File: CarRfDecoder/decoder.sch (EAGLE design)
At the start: 50 parts, among them T1 BC847, T2 BC847, T3 IRLML6402, U1 ATMEGA32U4TQFP-44, U2 RFM69CW, U3 MCP73831, U6 MIC5219 3.3V

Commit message: changes in the design
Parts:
- added C5, C6: 22pF, SparkFun-Capacitors:CAP0805
- added R12: 2K, SparkFun-Resistors:RESISTOR0603-RES
- added RST, XTAL, XTAL1: (no value), wirepad:SMD2
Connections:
- new net N$3: C5.2, U1.XTAL1, XTAL.P
- new net N$4: C6.2, U1.XTAL2, XTAL1.P
- new net N$5: R12.1, RST.P, U1.!RESET
- net GND: now also C5.1, C6.1
- net VCC: now also R12.2; no longer U1.!RESET
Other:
- moved on the sheet: C1
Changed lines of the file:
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@@
 <part name="SUPPLY1" library="SparkFun-Aesthetics" deviceset="VCC" device="" value="3.3V"/>
 <part name="AUX10" library="wirepad" deviceset="SMD2" device=""/>
+<part name="XTAL" library="wirepad" deviceset="SMD2" device=""/>
+<part name="XTAL1" library="wirepad" deviceset="SMD2" device=""/>
+<part name="C5" library="SparkFun-Capacitors" deviceset="CAP" device="0805" value="22pF"/>
+<part name="C6" library="SparkFun-Capacitors" deviceset="CAP" device="0805" value="22pF"/>
+<part name="GND3" library="SparkFun-Aesthetics" deviceset="GND" device=""/>
+<part name="R12" library="SparkFun-Resistors" deviceset="RESISTOR" device="0603-RES" value="2K"/>
+<part name="RST" library="wirepad" deviceset="SMD2" device=""/>
 </parts>
 <sheets>
@@
 <instance part="GND1" gate="1" x="20.32" y="10.16"/>
 <instance part="GND2" gate="1" x="20.32" y="27.94"/>
-<instance part="C1" gate="G$1" x="7.62" y="38.1"/>
+<instance part="C1" gate="G$1" x="-10.16" y="38.1"/>
 <instance part="USBV+" gate="1" x="-35.56" y="116.84"/>
 <instance part="USBD+" gate="1" x="-35.56" y="111.76"/>
@@
 <instance part="SUPPLY1" gate="G$1" x="27.94" y="-10.16"/>
 <instance part="AUX10" gate="1" x="220.98" y="-78.74" rot="MR0"/>
+<instance part="XTAL" gate="1" x="17.78" y="40.64"/>
+<instance part="XTAL1" gate="1" x="17.78" y="35.56"/>
+<instance part="C5" gate="G$1" x="10.16" y="43.18" rot="R90"/>
+<instance part="C6" gate="G$1" x="10.16" y="33.02" rot="R90"/>
+<instance part="GND3" gate="1" x="2.54" y="40.64"/>
+<instance part="R12" gate="G$1" x="30.48" y="96.52" rot="R90"/>
+<instance part="RST" gate="1" x="43.18" y="96.52" rot="R180"/>
 </instances>
 <busses>
@@
 <pinref part="U1" gate="G$1" pin="VCC@14"/>
 <wire x1="25.4" y1="83.82" x2="30.48" y2="83.82" width="0.1524" layer="91"/>
-<wire x1="25.4" y1="83.82" x2="25.4" y2="86.36" width="0.1524" layer="91"/>
 <junction x="25.4" y="83.82"/>
-<pinref part="U1" gate="G$1" pin="!RESET"/>
-<wire x1="25.4" y1="86.36" x2="30.48" y2="86.36" width="0.1524" layer="91"/>
 <wire x1="20.32" y1="83.82" x2="25.4" y2="83.82" width="0.1524" layer="91"/>
 <pinref part="U1" gate="G$1" pin="AVCC@24"/>
@@
 <junction x="25.4" y="81.28"/>
 <label x="15.24" y="86.36" size="1.778" layer="95"/>
+<pinref part="R12" gate="G$1" pin="2"/>
+<wire x1="30.48" y1="101.6" x2="25.4" y2="101.6" width="0.1524" layer="91"/>
+<wire x1="25.4" y1="101.6" x2="25.4" y2="83.82" width="0.1524" layer="91"/>
 </segment>
 <segment>
@@
 <pinref part="C1" gate="G$1" pin="2"/>
 <wire x1="30.48" y1="22.86" x2="20.32" y2="22.86" width="0.1524" layer="91"/>
-<wire x1="20.32" y1="22.86" x2="7.62" y2="22.86" width="0.1524" layer="91"/>
-<wire x1="7.62" y1="22.86" x2="7.62" y2="35.56" width="0.1524" layer="91"/>
+<wire x1="20.32" y1="22.86" x2="-10.16" y2="22.86" width="0.1524" layer="91"/>
+<wire x1="-10.16" y1="22.86" x2="-10.16" y2="35.56" width="0.1524" layer="91"/>
 <junction x="20.32" y="22.86"/>
 <wire x1="20.32" y1="22.86" x2="20.32" y2="15.24" width="0.1524" layer="91"/>
@@
 <pinref part="GND12" gate="1" pin="GND"/>
 </segment>
+<segment>
+<pinref part="C5" gate="G$1" pin="1"/>
+<pinref part="GND3" gate="1" pin="GND"/>
+<wire x1="5.08" y1="43.18" x2="2.54" y2="43.18" width="0.1524" layer="91"/>
+<pinref part="C6" gate="G$1" pin="1"/>
+<wire x1="5.08" y1="33.02" x2="5.08" y2="43.18" width="0.1524" layer="91"/>
+<junction x="5.08" y="43.18"/>
+</segment>
 </net>
 <net name="N$1" class="0">
@@
 <pinref part="U1" gate="G$1" pin="UCAP"/>
 <pinref part="C1" gate="G$1" pin="1"/>
-<wire x1="30.48" y1="58.42" x2="7.62" y2="58.42" width="0.1524" layer="91"/>
-<wire x1="7.62" y1="58.42" x2="7.62" y2="43.18" width="0.1524" layer="91"/>
+<wire x1="30.48" y1="58.42" x2="-10.16" y2="58.42" width="0.1524" layer="91"/>
+<wire x1="-10.16" y1="58.42" x2="-10.16" y2="43.18" width="0.1524" layer="91"/>
 </segment>
 </net>
@@
 </segment>
 </net>
+<net name="N$3" class="0">
+<segment>
+<pinref part="XTAL" gate="1" pin="P"/>
+<pinref part="U1" gate="G$1" pin="XTAL1"/>
+<wire x1="20.32" y1="40.64" x2="22.86" y2="40.64" width="0.1524" layer="91"/>
+<pinref part="C5" gate="G$1" pin="2"/>
+<wire x1="22.86" y1="40.64" x2="30.48" y2="40.64" width="0.1524" layer="91"/>
+<wire x1="12.7" y1="43.18" x2="22.86" y2="43.18" width="0.1524" layer="91"/>
+<wire x1="22.86" y1="43.18" x2="22.86" y2="40.64" width="0.1524" layer="91"/>
+<junction x="22.86" y="40.64"/>
+</segment>
+</net>
+<net name="N$4" class="0">
+<segment>
+<pinref part="XTAL1" gate="1" pin="P"/>
+<pinref part="U1" gate="G$1" pin="XTAL2"/>
+<wire x1="20.32" y1="35.56" x2="22.86" y2="35.56" width="0.1524" layer="91"/>
+<pinref part="C6" gate="G$1" pin="2"/>
+<wire x1="22.86" y1="35.56" x2="30.48" y2="35.56" width="0.1524" layer="91"/>
+<wire x1="12.7" y1="33.02" x2="22.86" y2="33.02" width="0.1524" layer="91"/>
+<wire x1="22.86" y1="33.02" x2="22.86" y2="35.56" width="0.1524" layer="91"/>
+<junction x="22.86" y="35.56"/>
+</segment>
+</net>
+<net name="N$5" class="0">
+<segment>
+<pinref part="R12" gate="G$1" pin="1"/>
+<pinref part="U1" gate="G$1" pin="!RESET"/>
+<wire x1="30.48" y1="91.44" x2="30.48" y2="86.36" width="0.1524" layer="91"/>
+<pinref part="RST" gate="1" pin="P"/>
+<wire x1="40.64" y1="96.52" x2="35.56" y2="96.52" width="0.1524" layer="91"/>
+<wire x1="35.56" y1="96.52" x2="35.56" y2="91.44" width="0.1524" layer="91"/>
+<wire x1="35.56" y1="91.44" x2="30.48" y2="91.44" width="0.1524" layer="91"/>
+<junction x="30.48" y="91.44"/>
+</segment>
+</net>

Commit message: Ready boards.
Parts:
- added VJ, VJ1: (no value), wirepad:SMD2
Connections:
- new net N$31: U2.3.3V, VJ.P
- net VCC: now also VJ1.P; no longer U2.3.3V
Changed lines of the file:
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@@
 <part name="R12" library="SparkFun-Resistors" deviceset="RESISTOR" device="0603-RES" value="2K"/>
 <part name="RST" library="wirepad" deviceset="SMD2" device=""/>
+<part name="VJ" library="wirepad" deviceset="SMD2" device=""/>
+<part name="VJ1" library="wirepad" deviceset="SMD2" device=""/>
 </parts>
 <sheets>
@@
 <instance part="R12" gate="G$1" x="30.48" y="96.52" rot="R90"/>
 <instance part="RST" gate="1" x="43.18" y="96.52" rot="R180"/>
+<instance part="VJ" gate="1" x="17.78" y="-15.24" rot="MR180"/>
+<instance part="VJ1" gate="1" x="17.78" y="-10.16" rot="MR180"/>
 </instances>
 <busses>
@@
 </segment>
 <segment>
-<pinref part="U2" gate="G$1" pin="3.3V"/>
-<wire x1="35.56" y1="-15.24" x2="27.94" y2="-15.24" width="0.1524" layer="91"/>
-<wire x1="27.94" y1="-15.24" x2="27.94" y2="-10.16" width="0.1524" layer="91"/>
+<pinref part="VJ1" gate="1" pin="P"/>
 <pinref part="SUPPLY1" gate="G$1" pin="VCC"/>
+<wire x1="20.32" y1="-10.16" x2="27.94" y2="-10.16" width="0.1524" layer="91"/>
 </segment>
 </net>
@@
 </segment>
 </net>
+<net name="N$31" class="0">
+<segment>
+<pinref part="U2" gate="G$1" pin="3.3V"/>
+<pinref part="VJ" gate="1" pin="P"/>
+<wire x1="20.32" y1="-15.24" x2="35.56" y2="-15.24" width="0.1524" layer="91"/>
+</segment>
+</net>

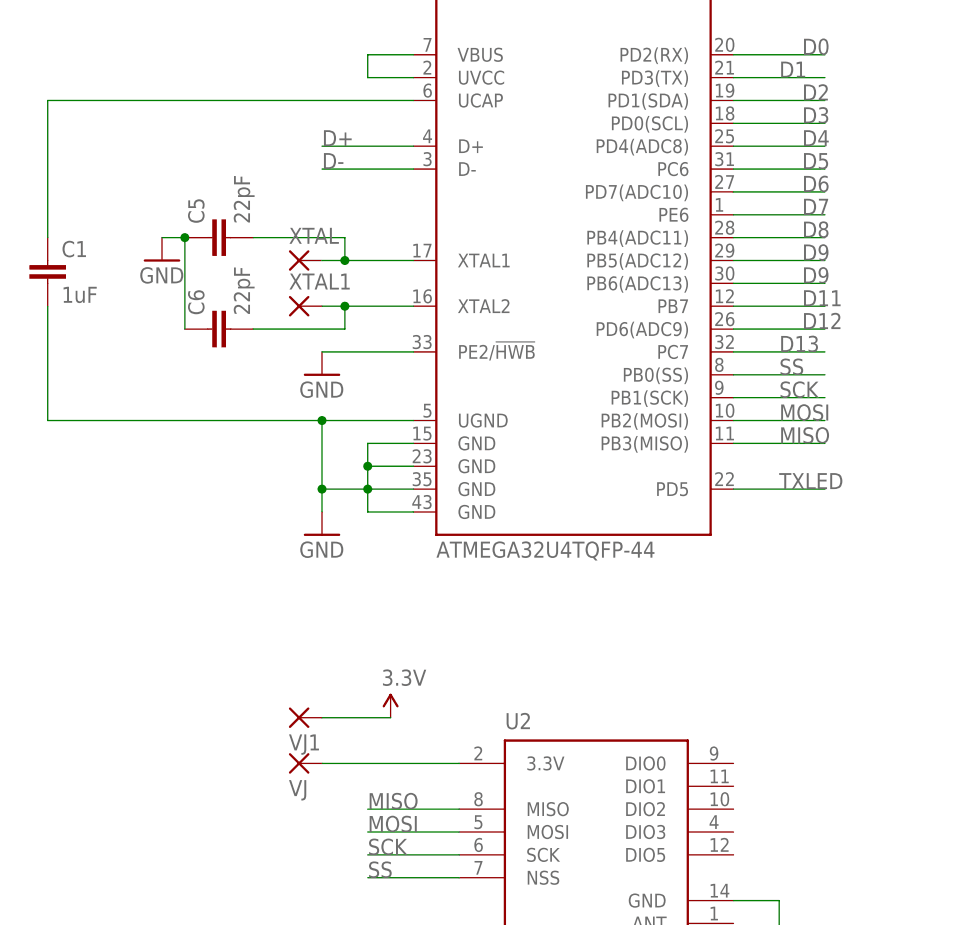
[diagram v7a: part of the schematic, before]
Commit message: Fix connection to the rf module and add a 16mhz crystal
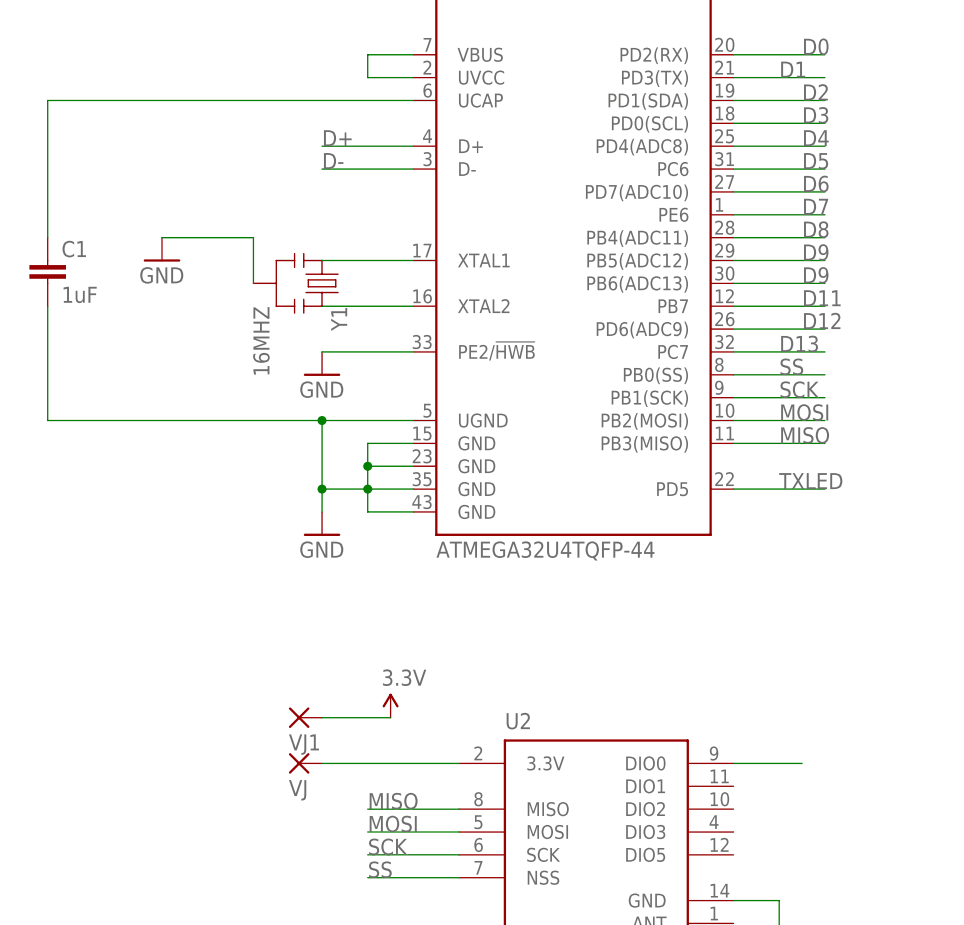
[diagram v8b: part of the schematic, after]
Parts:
- removed C5, C6: 22pF, SparkFun-Capacitors:CAP0805
- removed XTAL, XTAL1: (no value), wirepad:SMD2
- added Y1: 16MHZ, SparkFun-FreqCtrl:RESONATOR16MHZ
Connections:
- net D2: now also U2.DIO0
- net GND: now also Y1.2; no longer C5.1, C6.1
- net N$3: now also Y1.1; no longer C5.2, XTAL.P
- net N$4: now also Y1.3; no longer C6.2, XTAL1.P
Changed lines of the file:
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@@
 <part name="SUPPLY1" library="SparkFun-Aesthetics" deviceset="VCC" device="" value="3.3V"/>
 <part name="AUX10" library="wirepad" deviceset="SMD2" device=""/>
-<part name="XTAL" library="wirepad" deviceset="SMD2" device=""/>
-<part name="XTAL1" library="wirepad" deviceset="SMD2" device=""/>
-<part name="C5" library="SparkFun-Capacitors" deviceset="CAP" device="0805" value="22pF"/>
-<part name="C6" library="SparkFun-Capacitors" deviceset="CAP" device="0805" value="22pF"/>
 <part name="GND3" library="SparkFun-Aesthetics" deviceset="GND" device=""/>
 <part name="R12" library="SparkFun-Resistors" deviceset="RESISTOR" device="0603-RES" value="2K"/>
@@
 <part name="VJ" library="wirepad" deviceset="SMD2" device=""/>
 <part name="VJ1" library="wirepad" deviceset="SMD2" device=""/>
+<part name="Y1" library="SparkFun-FreqCtrl" deviceset="RESONATOR" device="16MHZ" value="16MHZ"/>
 </parts>
 <sheets>
@@
 <instance part="SUPPLY1" gate="G$1" x="27.94" y="-10.16"/>
 <instance part="AUX10" gate="1" x="220.98" y="-78.74" rot="MR0"/>
-<instance part="XTAL" gate="1" x="17.78" y="40.64"/>
-<instance part="XTAL1" gate="1" x="17.78" y="35.56"/>
-<instance part="C5" gate="G$1" x="10.16" y="43.18" rot="R90"/>
-<instance part="C6" gate="G$1" x="10.16" y="33.02" rot="R90"/>
 <instance part="GND3" gate="1" x="2.54" y="40.64"/>
 <instance part="R12" gate="G$1" x="30.48" y="96.52" rot="R90"/>
@@
 <instance part="VJ" gate="1" x="17.78" y="-15.24" rot="MR180"/>
 <instance part="VJ1" gate="1" x="17.78" y="-10.16" rot="MR180"/>
+<instance part="Y1" gate="G$1" x="20.32" y="38.1" rot="R270"/>
 </instances>
 <busses>
@@
 </segment>
 <segment>
-<pinref part="C5" gate="G$1" pin="1"/>
 <pinref part="GND3" gate="1" pin="GND"/>
-<wire x1="5.08" y1="43.18" x2="2.54" y2="43.18" width="0.1524" layer="91"/>
-<pinref part="C6" gate="G$1" pin="1"/>
-<wire x1="5.08" y1="33.02" x2="5.08" y2="43.18" width="0.1524" layer="91"/>
-<junction x="5.08" y="43.18"/>
+<pinref part="Y1" gate="G$1" pin="2"/>
+<wire x1="2.54" y1="43.18" x2="12.7" y2="43.18" width="0.1524" layer="91"/>
+<wire x1="12.7" y1="43.18" x2="12.7" y2="38.1" width="0.1524" layer="91"/>
 </segment>
 </net>
@@
 <wire x1="185.42" y1="25.4" x2="170.18" y2="25.4" width="0.1524" layer="91"/>
 <label x="172.72" y="25.4" size="1.778" layer="95"/>
+</segment>
+<segment>
+<pinref part="U2" gate="G$1" pin="DIO0"/>
+<wire x1="66.04" y1="-15.24" x2="73.66" y2="-15.24" width="0.1524" layer="91"/>
 </segment>
 </net>
@@
 <net name="N$3" class="0">
 <segment>
-<pinref part="XTAL" gate="1" pin="P"/>
 <pinref part="U1" gate="G$1" pin="XTAL1"/>
-<wire x1="20.32" y1="40.64" x2="22.86" y2="40.64" width="0.1524" layer="91"/>
-<pinref part="C5" gate="G$1" pin="2"/>
-<wire x1="22.86" y1="40.64" x2="30.48" y2="40.64" width="0.1524" layer="91"/>
-<wire x1="12.7" y1="43.18" x2="22.86" y2="43.18" width="0.1524" layer="91"/>
-<wire x1="22.86" y1="43.18" x2="22.86" y2="40.64" width="0.1524" layer="91"/>
-<junction x="22.86" y="40.64"/>
+<wire x1="20.32" y1="40.64" x2="30.48" y2="40.64" width="0.1524" layer="91"/>
+<pinref part="Y1" gate="G$1" pin="1"/>
 </segment>
 </net>
 <net name="N$4" class="0">
 <segment>
-<pinref part="XTAL1" gate="1" pin="P"/>
 <pinref part="U1" gate="G$1" pin="XTAL2"/>
-<wire x1="20.32" y1="35.56" x2="22.86" y2="35.56" width="0.1524" layer="91"/>
-<pinref part="C6" gate="G$1" pin="2"/>
-<wire x1="22.86" y1="35.56" x2="30.48" y2="35.56" width="0.1524" layer="91"/>
-<wire x1="12.7" y1="33.02" x2="22.86" y2="33.02" width="0.1524" layer="91"/>
-<wire x1="22.86" y1="33.02" x2="22.86" y2="35.56" width="0.1524" layer="91"/>
-<junction x="22.86" y="35.56"/>
-</segment>
-</net>
+<wire x1="20.32" y1="35.56" x2="30.48" y2="35.56" width="0.1524" layer="91"/>
+<pinref part="Y1" gate="G$1" pin="3"/>
+</segment>
+</net>
